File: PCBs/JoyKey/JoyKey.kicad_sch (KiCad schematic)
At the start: 6 parts, among them J1 OLED_DISPLAY, J3 Testpad wire hole1, U3 XIAO-RP2040-DIP, U4 LSM6DS3

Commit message: Updated BOM with LCSC parts
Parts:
- U4: LCSC (none) -> C967633
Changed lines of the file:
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@@
+			)
+		)
+		(property "LCSC" "C967633"
+			(at 135.89 161.29 0)
+			(effects
+				(font
+					(size 1.27 1.27)
+				)
+				(hide yes)
 			)
 		)

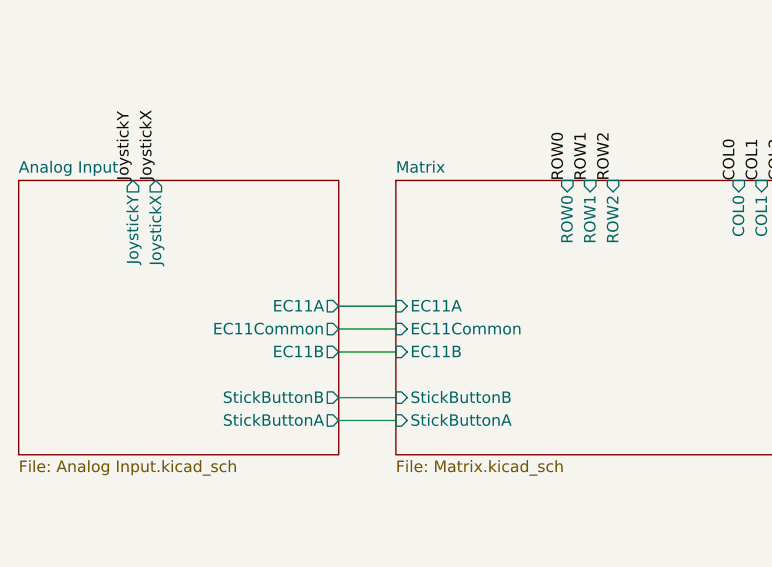
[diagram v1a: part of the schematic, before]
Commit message: Switched encoder to Alps SRBE110301 in sch
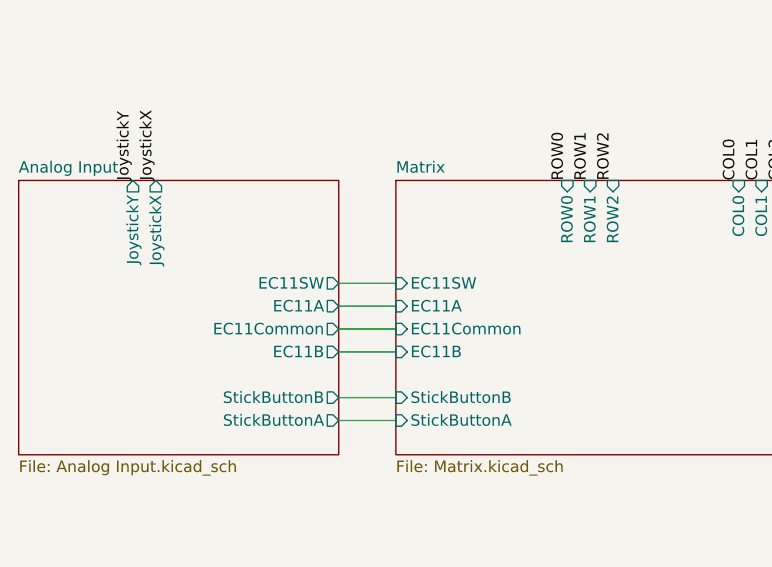
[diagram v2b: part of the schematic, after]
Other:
- sheet Analog Input ports: added EC11SW; removed none
- sheet Matrix ports: added EC11SW; removed none
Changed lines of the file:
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@@
+	(wire
+		(pts
+			(xy 78.74 115.57) (xy 85.09 115.57)
+		)
+		(stroke
+			(width 0)
+			(type default)
+		)
+	)
 	(wire
 		(pts
@@
 			)
 		)
+		(pin "EC11SW" input
+			(at 85.09 115.57 180)
+			(effects
+				(font
+					(size 1.27 1.27)
+				)
+				(justify left)
+			)
+		)
 		(instances
 			(project "JoyKey"
@@
 			(effects
 				(font
+					(size 1.27 1.27)
+				)
+				(justify right)
+			)
+		)
+		(pin "EC11SW" output
+			(at 78.74 115.57 0)
+			(effects
+				(font
